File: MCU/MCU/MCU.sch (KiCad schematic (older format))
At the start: 42 parts, among them J1 Conn_01x08, J2 Conn_01x08, J3 Conn_02x20_Odd_Even, J4 Conn_01x04, Q1 8050, U1 74HC04, U2 STM32F407VETx, Y1 12MHz

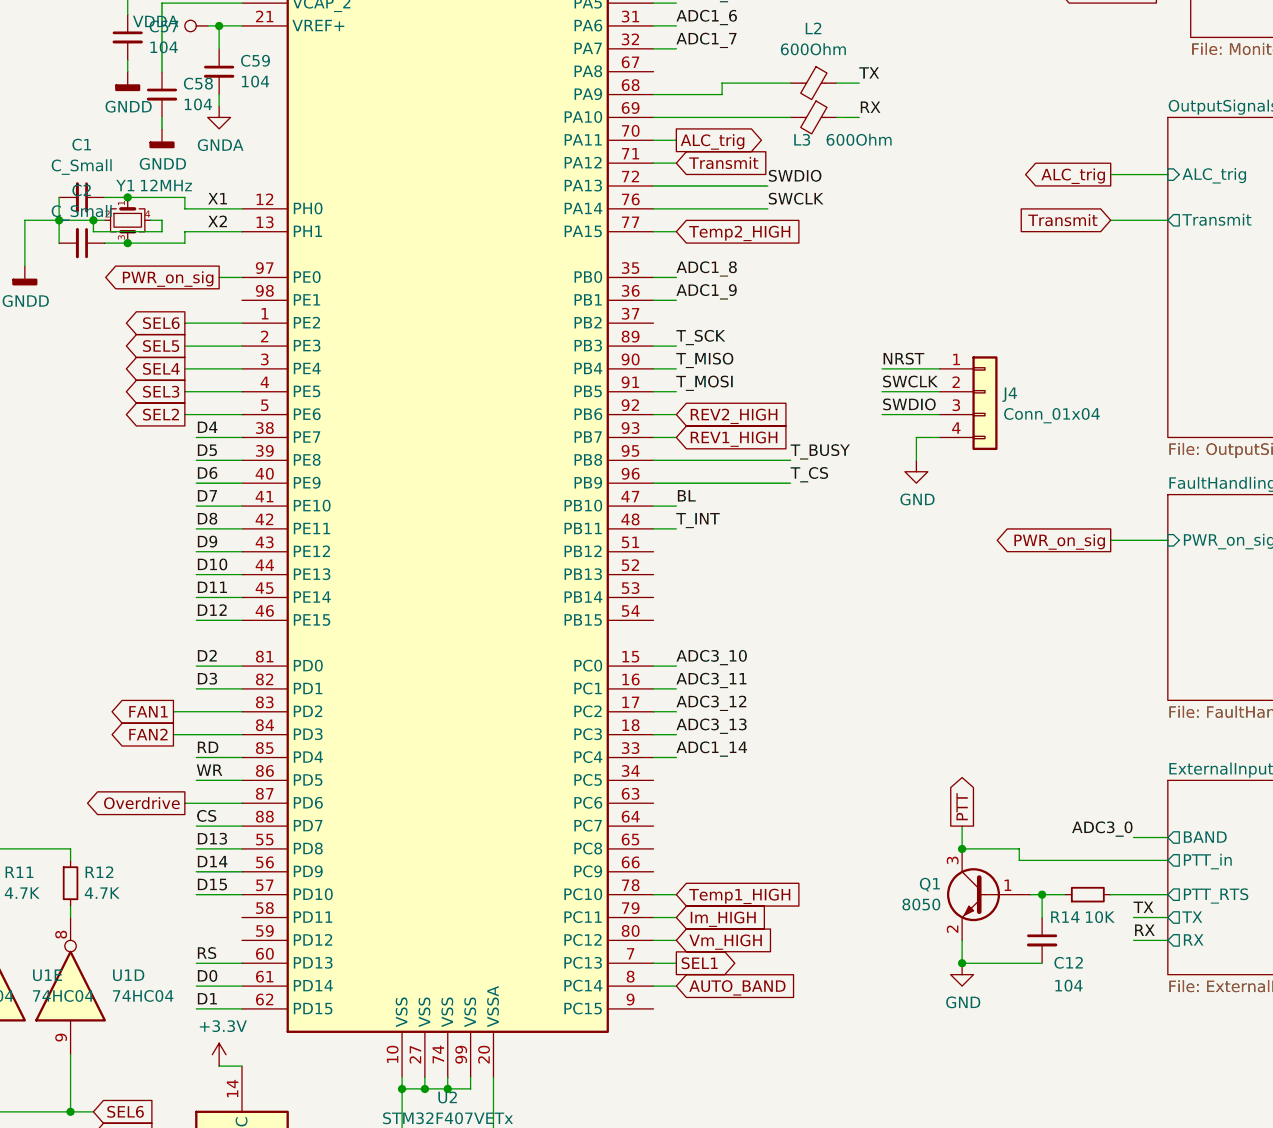
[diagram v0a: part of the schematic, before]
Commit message: MCU routed
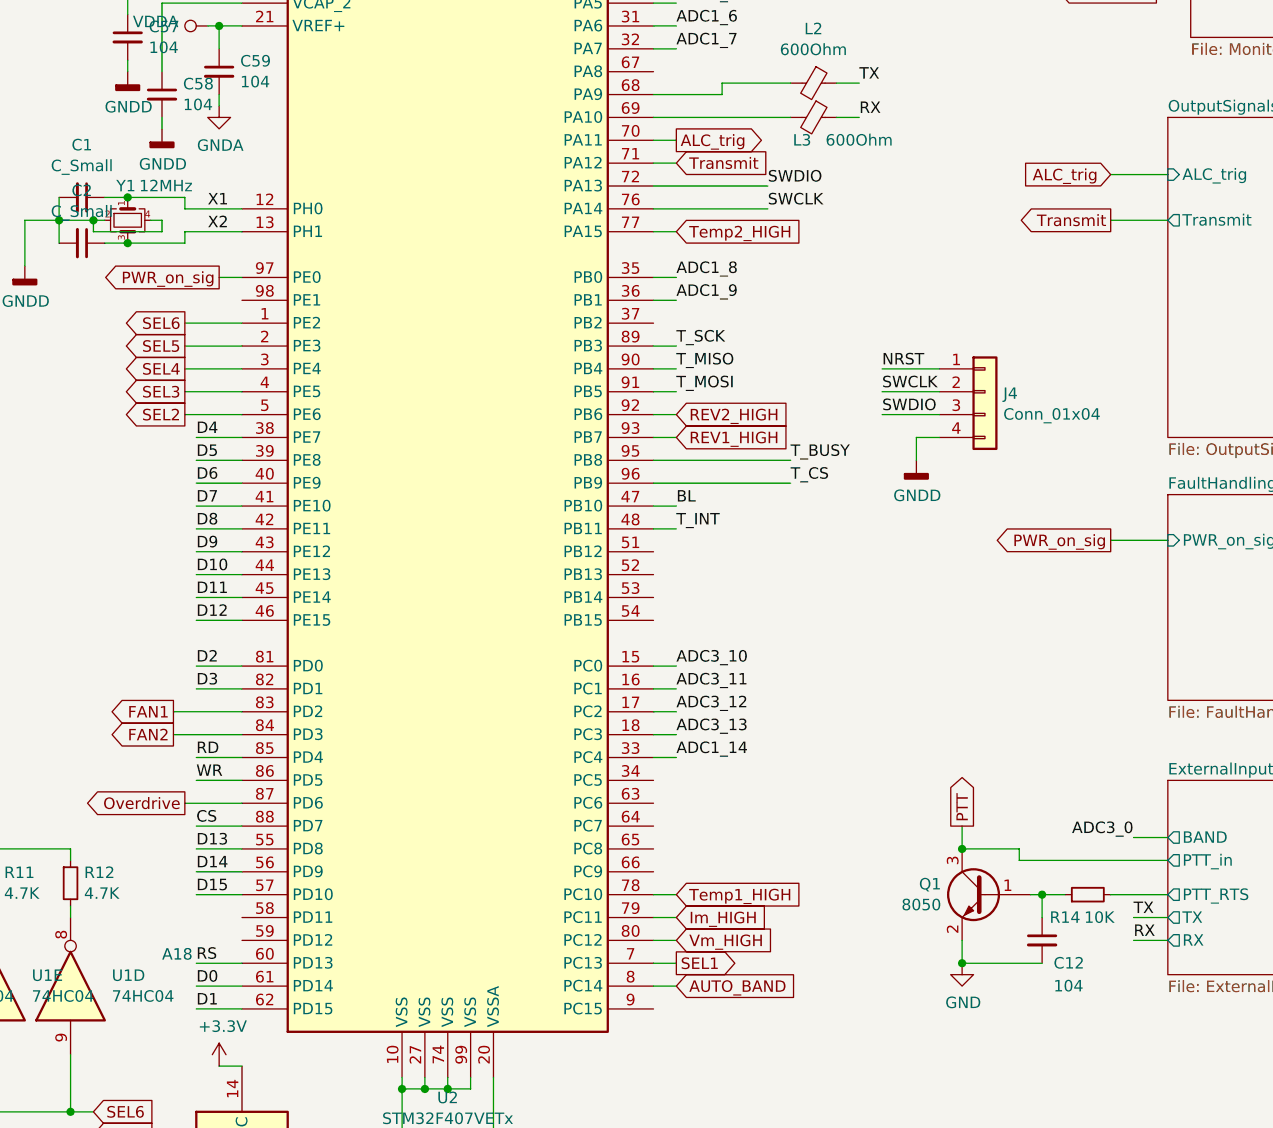
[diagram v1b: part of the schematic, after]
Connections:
- net GND: no longer J4.4 (Pin_4)
- net GNDD: now also J4.4 (Pin_4)
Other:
- note added: "A18"
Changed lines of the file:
@@
 Wire Wire Line
 	3300 1550 3350 1550
-Text GLabel 7700 2800 0    50   Output ~ 0
+Text GLabel 7700 2800 0    50   Input ~ 0
 ALC_trig
 Wire Wire Line
 	7700 2800 7950 2800
-Text GLabel 7700 3000 0    50   Input ~ 0
+Text GLabel 7700 3000 0    50   Output ~ 0
 Transmit
 Wire Wire Line
@@
 Wire Wire Line
 	6850 3950 6850 4050
-$Comp
-L power:GND #PWR017
-U 1 1 5F68FB04
-P 6850 4050
-F 0 "#PWR017" H 6850 3800 50  0001 C CNN
-F 1 "GND" H 6855 3877 50  0000 C CNN
-F 2 "" H 6850 4050 50  0001 C CNN
-F 3 "" H 6850 4050 50  0001 C CNN
-	1    6850 4050
-	1    0    0    -1
-$EndComp
 Text Label 3700 1550 0    50   ~ 0
 NRST
@@
 Wire Wire Line
 	6650 1550 6550 1550
+$Comp
+L power:GNDD #PWR0125
+U 1 1 5E46449F
+P 6850 4050
+F 0 "#PWR0125" H 6850 3800 50  0001 C CNN
+F 1 "GNDD" H 6854 3895 50  0000 C CNN
+F 2 "" H 6850 4050 50  0001 C CNN
+F 3 "" H 6850 4050 50  0001 C CNN
+	1    6850 4050
+	1    0    0    -1
+$EndComp
+Text Notes 3550 6250 0    50   ~ 0
+A18
 $EndSCHEMATC

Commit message: Power module
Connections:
- net CAN_RX: now reaches U2.51 (PB12)
- net CAN_TX: now reaches U2.52 (PB13)
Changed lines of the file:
@@
 F5 "TX" O L 7950 6050 50
 F6 "RX" O L 7950 6150 50
+F7 "CAN_TX" I R 10100 6150 50
+F8 "CAN_RX" O R 10100 6000 50
 $EndSheet
 Text Label 5800 1850 0    50   ~ 0
@@
 Text Notes 3550 6250 0    50   ~ 0
 A18
+Text Label 5800 4450 0    50   ~ 0
+CAN_RX
+Text Label 5800 4550 0    50   ~ 0
+CAN_TX
+Wire Wire Line
+	5800 4550 5700 4550
+Wire Wire Line
+	5700 4450 5800 4450
+Text Label 10200 6150 0    50   ~ 0
+CAN_TX
+Wire Wire Line
+	10200 6150 10100 6150
+Text Label 10200 6000 0    50   ~ 0
+CAN_RX
+Wire Wire Line
+	10200 6000 10100 6000
 $EndSCHEMATC
